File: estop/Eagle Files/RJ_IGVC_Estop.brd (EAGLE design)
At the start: 28 parts, among them T2 LD1086D2M33TR, U4 ATMEGA328P-AUR, X1 ICSP Connector, X2 1751248, X3 1751248, X4 1751248, X5 1751248

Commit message: fixed estop board
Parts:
- added U$2: (no value), RoboJackets-Aesthetics:ROBOBUZZ_0.8X
- moved C1 24.4 mm to (47.0, 15.2), turned to 180 degrees
- moved C3 5.68 mm to (59.7, 36.8)
- moved C4 2.84 mm to (55.9, 27.9), turned to 0 degrees
- moved R4 0.76 mm to (39.4, 40.1)
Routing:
- net CE: track 61.4 -> 24.9 mm, vias 8 -> 1
- net CSN: track 0.00 -> 26.8 mm, vias 0 -> 1
- net V_IN: track 32.2 -> 9.56 mm
- net IRQ: track 40.8 -> 24.6 mm, vias 9 -> 3
- net +3V3: track 0.42 -> 8.40 mm, vias 0 -> 4
- net N$5: track 37.5 -> 42.3 mm
- net N$9: track 18.6 -> 14.7 mm, vias 2 -> 1
- net GND: track 29.3 -> 32.3 mm, vias 12 -> 17
- net N$10: track 64.3 -> 63.0 mm, vias 4 -> 2
- net !RESET: track 57.9 -> 58.3 mm, vias 0 -> 2
- net BUTTON_LED: vias 2 -> 0

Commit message: estop diode magic
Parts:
- removed U$1: G5LE-14, IGVC-Misc:G5LE-14
- added D4, D5: HSMS-285K, avago:SOT363
- added D6, D7, D8: S10M-TP, IGVC-Discrete:SMC
- added J1: B2PS-VH(LF)(SN), RoboJackets-Connectors:B2PS-CENTERED
- added T1: TRANSISTOR, transistor:SC70
- added X6: S5B-PH-K-S(LF)(SN), IGVC-Misc:S5B-PH-SM4-TB(LF)(SN)
- JP1: value NRF24L01+PA+LNA -> (none)
- JP2: value Serial -> (none)
- U$2: device RoboJackets-Aesthetics:ROBOBUZZ_0.8X -> RoboJackets-Aesthetics:ROBOBUZZ_0.4X
- X1: value ICSP Connector -> 2X3SHROUDED
- moved U$2 47.8 mm to (25.0, 18.5)
- moved C6 45.2 mm to (3.30, 19.3), turned to 270 degrees
- moved S3 44.2 mm to (4.08, 26.6), turned to 90 degrees
- moved X1 42.5 mm to (5.35, 8.61)
- moved R2 41.4 mm to (5.68, 19.3)
- moved R4 34.8 mm to (9.50, 22.2)
- moved R1 34.3 mm to (18.1, 10.9), turned to 270 degrees
- moved X5 34.2 mm to (38.2, 4.58), turned to 0 degrees
- moved R6 33.8 mm to (9.50, 19.8)
- moved R5 32.6 mm to (9.49, 24.6)
- moved R3 32.6 mm to (40.7, 10.7), turned to 90 degrees
- moved C3 29.8 mm to (39.8, 14.6), turned to 0 degrees
- moved R10 29.2 mm to (29.3, 10.9)
- moved JP2 28.9 mm to (50.9, 37.6), turned to 90 degrees
- moved D1 28.6 mm to (20.2, 22.2)
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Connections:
- net +3V3 renamed +3.3V
- removed net N$10: U$1.P$2, U$1.P$4, X5.1
- removed net N$5: U$1.P$5, X5.2
- new net +24V: D6.A
- new net DIODE_TO_INTER: D7.C, X6.P$2
- new net DIODE_TO_RED: D6.C, X6.P$1
- new net ESTOP: J1.2
- new net N$1: T1.3, X5.2
- new net SOLENOID_TO_DIODE: D7.A, X6.P$3
- new net SOLENOID_TRIG: D8.C, X6.P$5
- new net SOLENOID_TRIG_GND: D8.A, X6.P$4
- new net VCC: D4.1, D4.6
- net GND: now also J1.1, R3.2, T1.2; no longer R3.1, U$1.P$1
- net OUT: now also R3.1, T1.1; no longer R3.2, U$1.P$3
- net V_IN: now also X5.1
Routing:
- net N$10: track 63.0 -> 0.00 mm, vias 2 -> 0
- net N$5: track 42.3 -> 0.00 mm
- net V_IN: track 9.56 -> 37.2 mm
- net MISO: track 50.1 -> 70.6 mm
- net SCK: track 48.0 -> 66.2 mm, vias 1 -> 2
- net N$6: track 23.7 -> 5.80 mm
- net OUT: track 32.5 -> 15.7 mm, vias 7 -> 2
- net MOSI: track 47.7 -> 62.3 mm
- net BUTTON_LED: track 7.97 -> 22.6 mm, vias 0 -> 2
- net CSN: track 26.8 -> 14.2 mm, vias 1 -> 0
- net WIRELESS_LED: track 6.71 -> 19.2 mm
- net N$9: track 14.7 -> 2.51 mm, vias 1 -> 0
- net !RESET: track 58.3 -> 69.2 mm, vias 2 -> 4
- net CE: track 24.9 -> 15.8 mm, vias 1 -> 0
- net +3.3V: track 8.40 -> 0.00 mm, vias 4 -> 0
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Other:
- board outline added: 57 x 46 mm
- board text added: "24V BTN"
- board text added: "24V OUT"
- board text added: "3.3V BTN"
- board text added: "Button"
- board text added: "E-Stop Board v1.1"
- board text added: "GND"
- board text added: "I/O"
- board text added: "Power"
- board text added: "Radio"
- board text added: "Wireless"

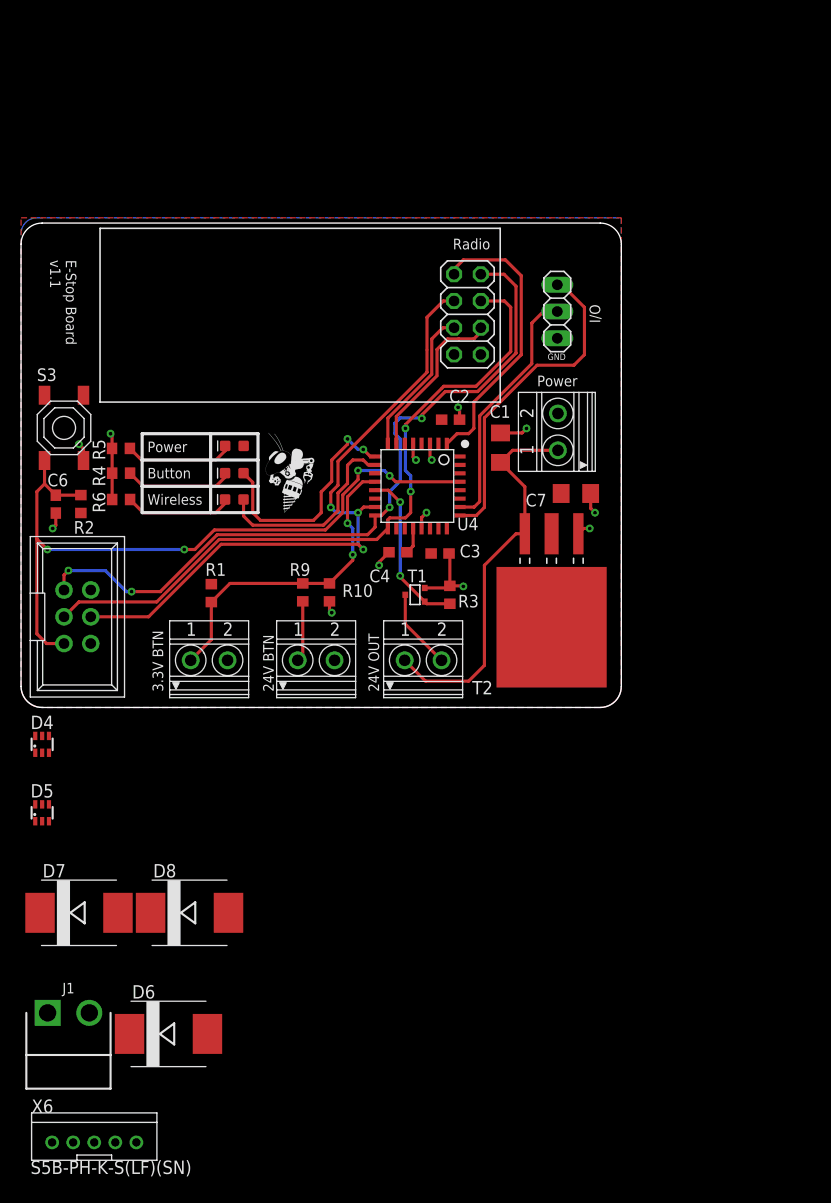
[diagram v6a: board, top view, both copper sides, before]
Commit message: Revert "estop diode magic"
This reverts commit 0d0471845709adb358787b62836d6b2af97c87b1.
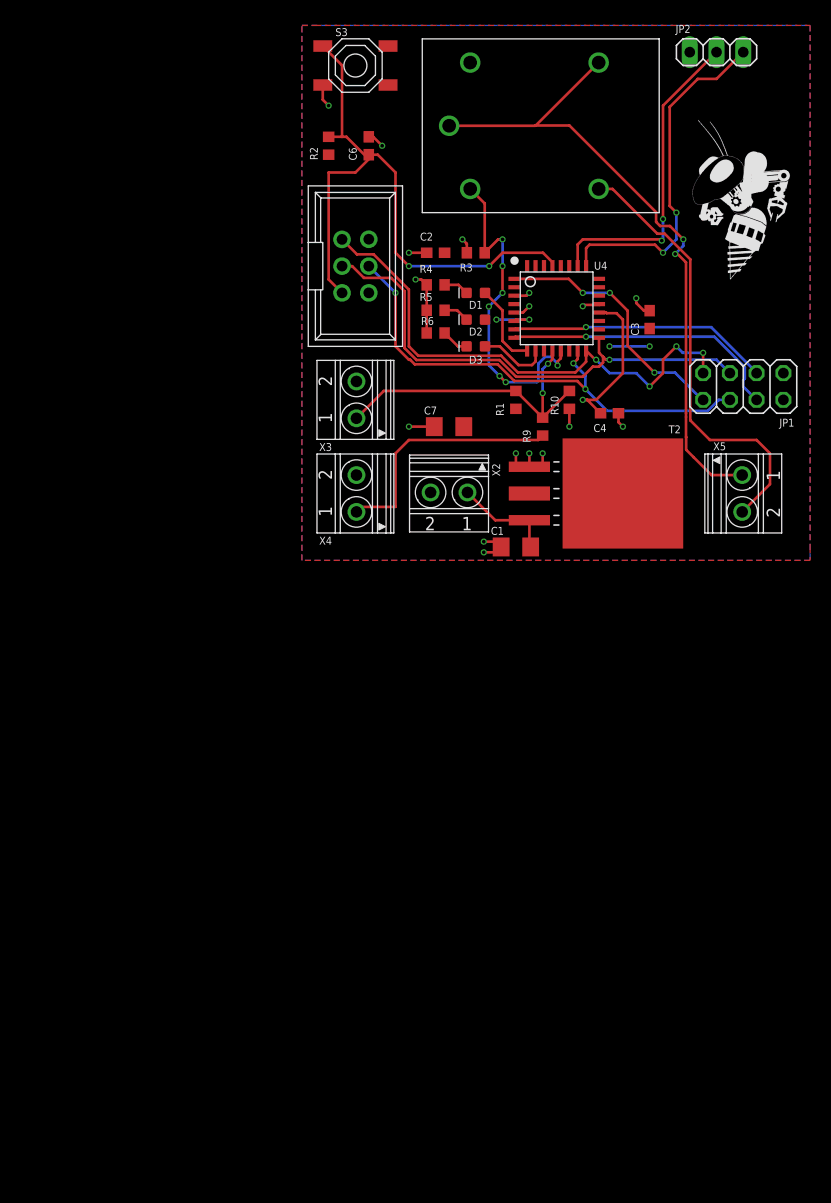
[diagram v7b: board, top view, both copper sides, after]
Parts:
- removed D4, D5: HSMS-285K, avago:SOT363
- removed D6, D7, D8: S10M-TP, IGVC-Discrete:SMC
- removed J1: B2PS-VH(LF)(SN), RoboJackets-Connectors:B2PS-CENTERED
- removed T1: TRANSISTOR, transistor:SC70
- removed X6: S5B-PH-K-S(LF)(SN), IGVC-Misc:S5B-PH-SM4-TB(LF)(SN)
- added U$1: G5LE-14, IGVC-Misc:G5LE-14
- JP1: value (none) -> NRF24L01+PA+LNA
- JP2: value (none) -> Serial
- U$2: device RoboJackets-Aesthetics:ROBOBUZZ_0.4X -> RoboJackets-Aesthetics:ROBOBUZZ_0.8X
- X1: value 2X3SHROUDED -> ICSP Connector
- moved U$2 47.8 mm to (67.3, 40.6)
- moved C6 45.2 mm to (33.0, 53.3), turned to 90 degrees
- moved S3 44.2 mm to (31.8, 61.0), turned to 0 degrees
- moved X1 42.5 mm to (31.8, 41.9)
- moved R2 41.4 mm to (29.2, 53.3)
- moved R4 34.8 mm to (39.4, 40.1)
- moved R1 34.3 mm to (47.0, 29.2), turned to 90 degrees
- moved X5 34.2 mm to (68.6, 20.3), turned to 270 degrees
- moved R6 33.8 mm to (39.4, 35.6)
- moved R5 32.6 mm to (39.4, 37.7)
- moved R3 32.6 mm to (43.2, 43.2), turned to 0 degrees
- moved C3 29.8 mm to (59.7, 36.8), turned to 90 degrees
- moved R10 29.2 mm to (52.1, 29.2)
- moved JP2 28.9 mm to (66.0, 62.2), turned to 0 degrees
- moved D1 28.6 mm to (43.2, 39.4)
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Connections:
- net +3.3V renamed +3V3
- removed net +24V: D6.A
- removed net DIODE_TO_INTER: D7.C, X6.P$2
- removed net DIODE_TO_RED: D6.C, X6.P$1
- removed net ESTOP: J1.2
- removed net N$1: T1.3, X5.2
- removed net SOLENOID_TO_DIODE: D7.A, X6.P$3
- removed net SOLENOID_TRIG: D8.C, X6.P$5
- removed net SOLENOID_TRIG_GND: D8.A, X6.P$4
- removed net VCC: D4.1, D4.6
- new net N$10: U$1.P$2, U$1.P$4, X5.1
- new net N$5: U$1.P$5, X5.2
- net GND: now also R3.1, U$1.P$1; no longer J1.1, R3.2, T1.2
- net OUT: now also R3.2, U$1.P$3; no longer R3.1, T1.1
- net V_IN: no longer X5.1
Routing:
- net N$10: track 0.00 -> 63.0 mm, vias 0 -> 2
- net N$5: track 0.00 -> 42.3 mm
- net V_IN: track 37.2 -> 9.56 mm
- net MISO: track 70.6 -> 50.1 mm
- net SCK: track 66.2 -> 48.0 mm, vias 2 -> 1
- net N$6: track 5.80 -> 23.7 mm
- net OUT: track 15.7 -> 32.5 mm, vias 2 -> 7
- net MOSI: track 62.3 -> 47.7 mm
- net BUTTON_LED: track 22.6 -> 7.97 mm, vias 2 -> 0
- net CSN: track 14.2 -> 26.8 mm, vias 0 -> 1
- net WIRELESS_LED: track 19.2 -> 6.71 mm
- net N$9: track 2.51 -> 14.7 mm, vias 0 -> 1
- net !RESET: track 69.2 -> 58.3 mm, vias 4 -> 2
- net CE: track 15.8 -> 24.9 mm, vias 0 -> 1
- net +3V3: track 0.00 -> 8.40 mm, vias 0 -> 4
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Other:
- board outline removed
- board text removed: "24V BTN"
- board text removed: "24V OUT"
- board text removed: "3.3V BTN"
- board text removed: "Button"
- board text removed: "E-Stop Board v1.1"
- board text removed: "GND"
- board text removed: "I/O"
- board text removed: "Power"
- board text removed: "Radio"
- board text removed: "Wireless"

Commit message: Diode magic
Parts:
- added D12, D13, D14: S10M-TP, IGVC-Discrete:SMC
- added J2: B2PS-VH(LF)(SN), RoboJackets-Connectors:B2PS-CENTERED
- added X12: S5B-PH-K-S(LF)(SN), IGVC-Misc:S5B-PH-SM4-TB(LF)(SN)
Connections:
- new net +24V: D12.A
- new net DIODE_TO_INTER: D13.C, X12.P$2
- new net DIODE_TO_RED: D12.C, X12.P$1
- new net ESTOP: J2.2
- new net SOLENOID_TO_DIODE: D13.A, X12.P$3
- new net SOLENOID_TRIG: D14.C, X12.P$5
- new net SOLENOID_TRIG_GND: D14.A, X12.P$4
- net GND: now also J2.1
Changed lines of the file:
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@@
 <?xml version="1.0" encoding="utf-8"?>
 <!DOCTYPE eagle SYSTEM "eagle.dtd">
-<eagle version="9.1.1">
+<eagle version="9.1.3">
 <drawing>
 <settings>
@@
 <element name="R2" library="rcl" library_urn="urn:adsk.eagle:library:334" package="R0603" package3d_urn="urn:adsk.eagle:package:23555/2" value="10k" x="29.21" y="53.34" smashed="yes" rot="R270">
 <attribute name="NAME" x="27.432" y="53.213" size="0.75" layer="25" rot="R270"/>
-<attribute name="SPICEPREFIX" value="R" x="29.21" y="53.34" size="1.778" layer="27" rot="R270" display="off"/>
 </element>
 <element name="R3" library="resistor" library_urn="urn:adsk.eagle:library:348" package="R0603" package3d_urn="urn:adsk.eagle:package:26057/1" value="10k" x="43.18" y="43.18" smashed="yes">
@@
 </element>
 <element name="U$2" library="RoboJackets-Aesthetics" package="ROBOBUZZ_0.8X" value="" x="67.31" y="40.64"/>
+<element name="D12" library="IGVC-Discrete" package="SMC" value="S10M-TP" x="41.91" y="7.62"/>
+<element name="D13" library="IGVC-Discrete" package="SMC" value="S10M-TP" x="66.04" y="7.62"/>
+<element name="D14" library="IGVC-Discrete" package="SMC" value="S10M-TP" x="77.47" y="7.62"/>
+<element name="J2" library="RoboJackets-Connectors" package="B2PS-CENTERED" value="B2PS-VH(LF)(SN)" x="31.75" y="11.43">
+<attribute name="DIGIKEY" value="455-1648-ND" x="-12.7" y="35.56" size="1.778" layer="27" display="off"/>
+<attribute name="MPN" value="B2PS-VH(LF)(SN)" x="-12.7" y="35.56" size="1.778" layer="27" display="off"/>
+</element>
+<element name="X12" library="IGVC-Misc" package="S5B-PH-SM4-TB(LF)(SN)" value="S5B-PH-K-S(LF)(SN)" x="48.26" y="5.08"/>
 </elements>
 <signals>
@@
 <wire x1="46.99" y1="24.13" x2="46.99" y2="22.86" width="0.254" layer="1"/>
 <wire x1="49.53" y1="24.13" x2="49.53" y2="22.86" width="0.254" layer="1"/>
+<contactref element="J2" pad="1"/>
+<wire x1="31.85" y1="22.07" x2="29.77" y2="11.43" width="0" layer="19" extent="1-1"/>
 </signal>
 <signal name="MISO">
@@
 <polygon width="0.1524" layer="1">
 <vertex x="27.94" y="64.77"/>
-<vertex x="74.93" y="64.77"/>
-<vertex x="74.93" y="15.24"/>
-<vertex x="74.93" y="13.97"/>
-<vertex x="26.67" y="13.97"/>
+<vertex x="83.82" y="64.77"/>
+<vertex x="83.82" y="0"/>
+<vertex x="26.67" y="0"/>
 <vertex x="26.67" y="64.77"/>
 </polygon>
@@
 <wire x1="55.88" y1="34.29" x2="59.69" y2="34.29" width="0.254" layer="16"/>
 </signal>
+<signal name="DIODE_TO_RED">
+<contactref element="D12" pad="C"/>
+<contactref element="X12" pad="P$1"/>
+<wire x1="38.21" y1="7.62" x2="50.21" y2="6.78" width="0" layer="19" extent="1-1"/>
+</signal>
+<signal name="DIODE_TO_INTER">
+<contactref element="D13" pad="C"/>
+<contactref element="X12" pad="P$2"/>
+<wire x1="52.21" y1="6.78" x2="62.34" y2="7.62" width="0" layer="19" extent="1-1"/>
+</signal>
+<signal name="SOLENOID_TRIG">
+<contactref element="D14" pad="C"/>
+<contactref element="X12" pad="P$5"/>
+<wire x1="58.21" y1="6.78" x2="73.77" y2="7.62" width="0" layer="19" extent="1-1"/>
+</signal>
+<signal name="+24V">
+<contactref element="D12" pad="A"/>
+</signal>
+<signal name="SOLENOID_TO_DIODE">
+<contactref element="D13" pad="A"/>
+<contactref element="X12" pad="P$3"/>
+<wire x1="54.21" y1="6.78" x2="69.74" y2="7.62" width="0" layer="19" extent="1-1"/>
+</signal>
+<signal name="SOLENOID_TRIG_GND">
+<contactref element="D14" pad="A"/>
+<contactref element="X12" pad="P$4"/>
+<wire x1="56.21" y1="6.78" x2="81.17" y2="7.62" width="0" layer="19" extent="1-1"/>
+</signal>
+<signal name="ESTOP">
+<contactref element="J2" pad="2"/>
+</signal>
 </signals>
